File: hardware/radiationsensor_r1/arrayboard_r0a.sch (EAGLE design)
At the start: 19 parts, among them CN0 RADIATION-SENSOR-REV1, CN1 RADIATION-SENSOR-REV1, CN10 RADIATION-SENSOR-REV1, CN11 RADIATION-SENSOR-REV1, CN12 RADIATION-SENSOR-REV1, CN13 RADIATION-SENSOR-REV1, CN14 RADIATION-SENSOR-REV1, CN15 RADIATION-SENSOR-REV1, CN2 RADIATION-SENSOR-REV1, CN3 RADIATION-SENSOR-REV1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

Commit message: basic layout (not including microcontroller)
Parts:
- removed U$17: ARDUINO_PRO_MINI, SparkFun-Boards:ARDUINO_PRO_MINI
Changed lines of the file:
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@@
 <layer number="54" name="bGND_GNDA" color="1" fill="9" visible="no" active="no"/>
 <layer number="56" name="wert" color="7" fill="1" visible="no" active="no"/>
+<layer number="57" name="tCAD" color="7" fill="1" visible="no" active="no"/>
 <layer number="91" name="Nets" color="2" fill="1" visible="yes" active="yes"/>
 <layer number="92" name="Busses" color="1" fill="1" visible="yes" active="yes"/>
@@
 <layer number="132" name="bAdjust" color="7" fill="1" visible="yes" active="yes"/>
 <layer number="144" name="Drill_legend" color="7" fill="1" visible="no" active="yes"/>
+<layer number="150" name="Notes" color="7" fill="1" visible="no" active="yes"/>
 <layer number="151" name="HeatSink" color="7" fill="1" visible="no" active="yes"/>
 <layer number="152" name="_bDocu" color="7" fill="1" visible="yes" active="yes"/>
+<layer number="153" name="FabDoc1" color="6" fill="1" visible="no" active="no"/>
+<layer number="154" name="FabDoc2" color="2" fill="1" visible="no" active="no"/>
+<layer number="155" name="FabDoc3" color="7" fill="15" visible="no" active="no"/>
 <layer number="199" name="Contour" color="7" fill="1" visible="yes" active="yes"/>
 <layer number="200" name="200bmp" color="1" fill="10" visible="no" active="yes"/>
@@
 <part name="CN14" library="openct" deviceset="RADIATION-SENSOR-REV1" device=""/>
 <part name="CN15" library="openct" deviceset="RADIATION-SENSOR-REV1" device=""/>
-<part name="U$17" library="SparkFun-Boards" deviceset="ARDUINO_PRO_MINI" device=""/>
 <part name="GND1" library="openct" deviceset="GND" device=""/>
 <part name="GND2" library="openct" deviceset="GND" device=""/>
@@
 <instance part="CN14" gate="G$1" x="78.74" y="-198.12"/>
 <instance part="CN15" gate="G$1" x="78.74" y="-236.22"/>
-<instance part="U$17" gate="G$1" x="-63.5" y="25.4"/>
 <instance part="GND1" gate="1" x="50.8" y="12.7"/>
 <instance part="GND2" gate="1" x="114.3" y="12.7"/>

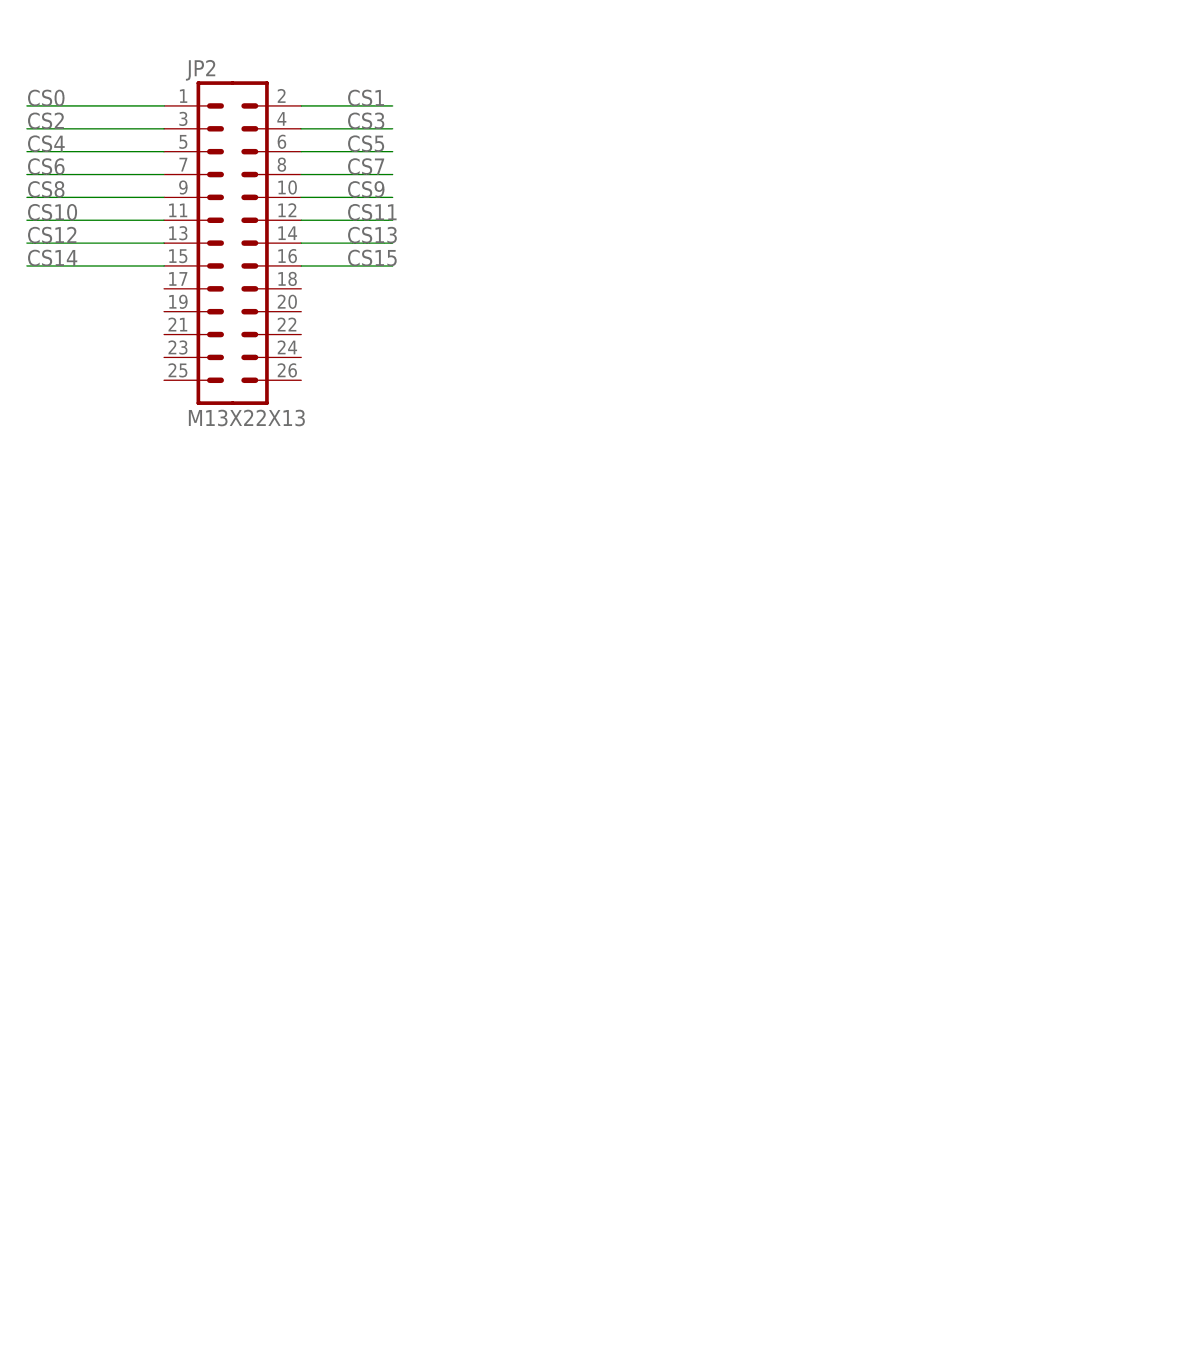
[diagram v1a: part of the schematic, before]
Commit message: Added connector an IO expander
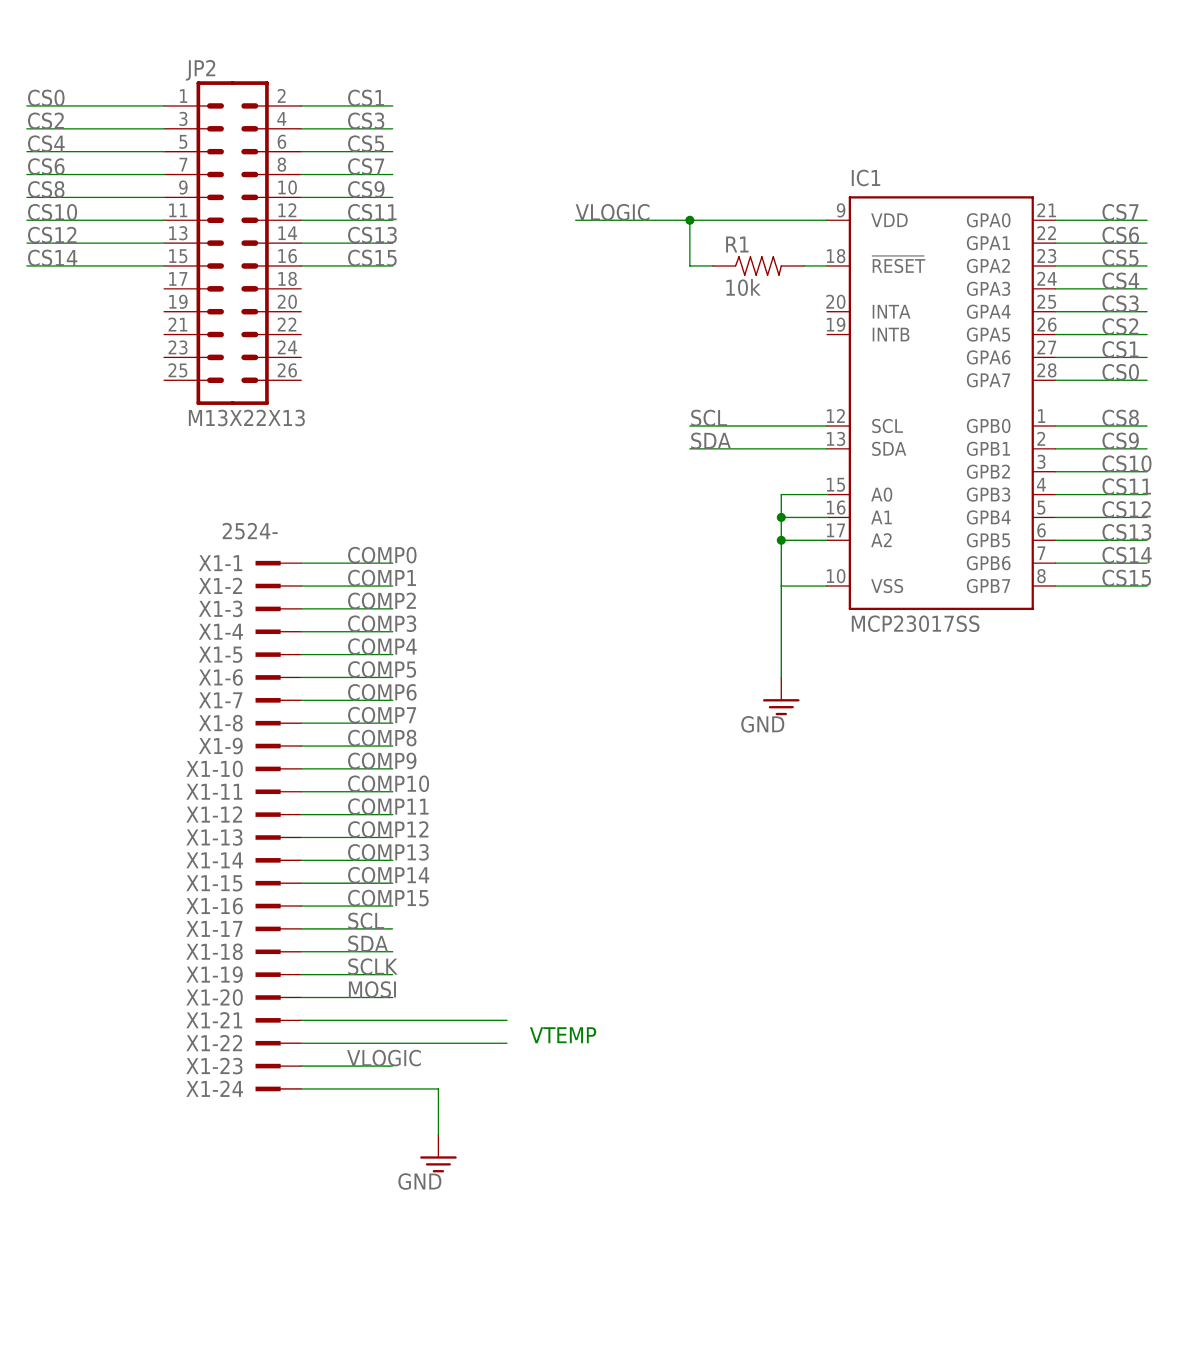
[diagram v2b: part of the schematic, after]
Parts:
- added IC1: MCP23017SS, adafruit:MCP23017SS
- added R1: 10k, openct:RESISTOR0603
- added X1: 2524-, con-3m:2524-
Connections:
- new net N$19: X1-21.KL
- new net N$2: IC1.!RESET, R1.2
- new net N$20: X1-22.KL
- new net SCL: IC1.SCL, X1-17.KL
- new net SDA: IC1.SDA, X1-18.KL
- new net VLOGIC: IC1.VDD, R1.1, X1-23.KL
- net COMP0: now also X1-1.KL
- net COMP1: now also X1-2.KL
- net COMP10: now also X1-11.KL
- net COMP11: now also X1-12.KL
- net COMP12: now also X1-13.KL
- net COMP13: now also X1-14.KL
- net COMP14: now also X1-15.KL
- net COMP15: now also X1-16.KL
- net COMP2: now also X1-3.KL
- net COMP3: now also X1-4.KL
- net COMP4: now also X1-5.KL
- net COMP5: now also X1-6.KL
- net COMP6: now also X1-7.KL
- net COMP7: now also X1-8.KL
- net COMP8: now also X1-9.KL
- net COMP9: now also X1-10.KL
- net CS0: now also IC1.GPA7
- net CS1: now also IC1.GPA6
- net CS10: now also IC1.GPB2
- net CS11: now also IC1.GPB3
- net CS12: now also IC1.GPB4
- net CS13: now also IC1.GPB5
- net CS14: now also IC1.GPB6
- net CS15: now also IC1.GPB7
- net CS2: now also IC1.GPA5
- net CS3: now also IC1.GPA4
- net CS4: now also IC1.GPA3
- net CS5: now also IC1.GPA2
- net CS6: now also IC1.GPA1
- net CS7: now also IC1.GPA0
- net CS8: now also IC1.GPB0
- net CS9: now also IC1.GPB1
- net GND: now also IC1.A0, IC1.A1, IC1.A2, IC1.VSS, X1-24.KL
- net MOSI: now also X1-20.KL
- net SCLK: now also X1-19.KL
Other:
- note added: "VTEMP"

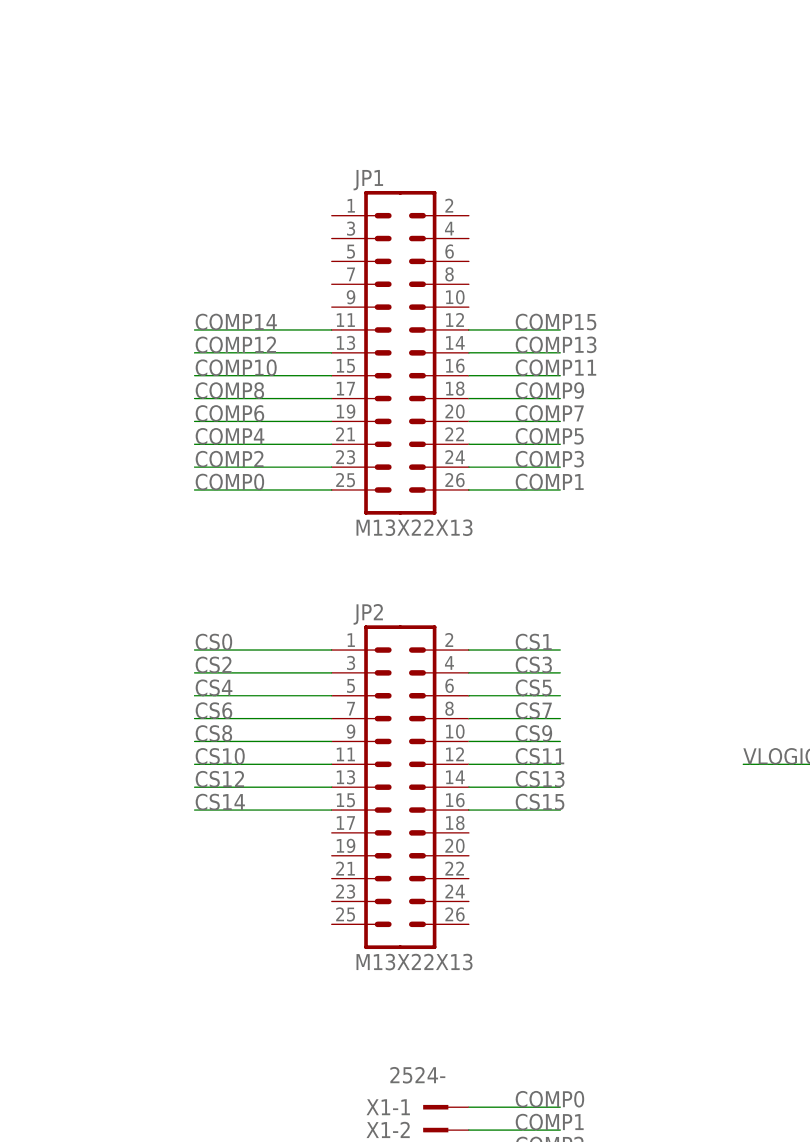
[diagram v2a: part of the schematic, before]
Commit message: connector and IO expander nearly wired
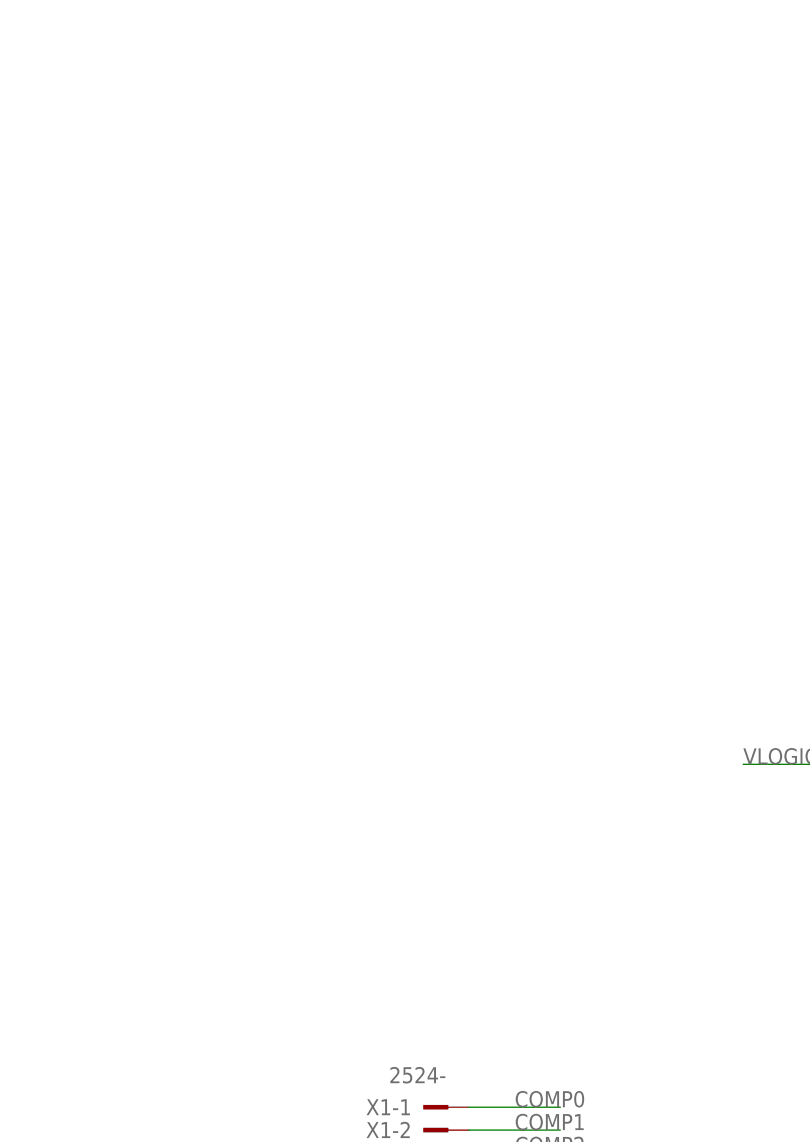
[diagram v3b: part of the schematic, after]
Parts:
- removed JP1, JP2: M13X22X13, SparkFun-Connectors:M13X22X13
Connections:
- net COMP0: no longer JP1.25
- net COMP1: no longer JP1.26
- net COMP10: no longer JP1.15
- net COMP11: no longer JP1.16
- net COMP12: no longer JP1.13
- net COMP13: no longer JP1.14
- net COMP14: no longer JP1.11
- net COMP15: no longer JP1.12
- net COMP2: no longer JP1.23
- net COMP3: no longer JP1.24
- net COMP4: no longer JP1.21
- net COMP5: no longer JP1.22
- net COMP6: no longer JP1.19
- net COMP7: no longer JP1.20
- net COMP8: no longer JP1.17
- net COMP9: no longer JP1.18
- net CS0: no longer JP2.1
- net CS1: no longer JP2.2
- net CS10: no longer JP2.11
- net CS11: no longer JP2.12
- net CS12: no longer JP2.13
- net CS13: no longer JP2.14
- net CS14: no longer JP2.15
- net CS15: no longer JP2.16
- net CS2: no longer JP2.3
- net CS3: no longer JP2.4
- net CS4: no longer JP2.5
- net CS5: no longer JP2.6
- net CS6: no longer JP2.7
- net CS7: no longer JP2.8
- net CS8: no longer JP2.9
- net CS9: no longer JP2.10

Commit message: basic layout complete
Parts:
- added C1: (no value), openct:CAP0603
- added X2: 22-23-2041, con-molex:22-23-2041
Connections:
- removed net N$19: X1-21.KL
- removed net N$20: X1-22.KL
- new net VTEMP11: CN11.VTEMP, X1-22.KL
- new net VTEMP4: CN4.VTEMP, X1-21.KL
- net 5V: now also X2-1.S
- net GND: now also C1.2, X2-2.S, X2-3.S
- net VBIAS: now also X2-4.S
- net VLOGIC: now also C1.1
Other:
- note removed: "VTEMP"
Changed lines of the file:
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@@
 <part name="GND18" library="openct" deviceset="GND" device=""/>
 <part name="R1" library="openct" deviceset="RESISTOR" device="0603" value="10k"/>
+<part name="C1" library="openct" deviceset="CAP" device="0603"/>
+<part name="GND19" library="openct" deviceset="GND" device=""/>
+<part name="X2" library="con-molex" deviceset="22-23-2041" device=""/>
+<part name="U$17" library="openct" deviceset="VBIAS" device=""/>
+<part name="U$34" library="openct" deviceset="5V" device=""/>
+<part name="GND20" library="openct" deviceset="GND" device=""/>
 </parts>
 <sheets>
 <sheet>
 <plain>
-<text x="231.14" y="-205.74" size="1.778" layer="91">VTEMP</text>
 </plain>
 <instances>
@@
 <instance part="GND18" gate="1" x="259.08" y="-167.64"/>
 <instance part="R1" gate="G$1" x="256.54" y="-119.38"/>
+<instance part="C1" gate="G$1" x="241.3" y="-119.38"/>
+<instance part="GND19" gate="1" x="241.3" y="-124.46"/>
+<instance part="X2" gate="-1" x="200.66" y="-248.92" rot="R180"/>
+<instance part="X2" gate="-2" x="200.66" y="-246.38" rot="R180"/>
+<instance part="X2" gate="-3" x="200.66" y="-243.84" rot="R180"/>
+<instance part="X2" gate="-4" x="200.66" y="-241.3" rot="R180"/>
+<instance part="U$17" gate="G$1" x="208.28" y="-236.22"/>
+<instance part="U$34" gate="G$1" x="208.28" y="-254" rot="R180"/>
+<instance part="GND20" gate="1" x="220.98" y="-254"/>
 </instances>
 <busses>
@@
 <junction x="259.08" y="-149.86"/>
 </segment>
+<segment>
+<pinref part="C1" gate="G$1" pin="2"/>
+<pinref part="GND19" gate="1" pin="GND"/>
+</segment>
+<segment>
+<pinref part="X2" gate="-2" pin="S"/>
+<wire x1="203.2" y1="-246.38" x2="208.28" y2="-246.38" width="0.1524" layer="91"/>
+<wire x1="208.28" y1="-246.38" x2="208.28" y2="-243.84" width="0.1524" layer="91"/>
+<wire x1="208.28" y1="-243.84" x2="220.98" y2="-243.84" width="0.1524" layer="91"/>
+<wire x1="220.98" y1="-243.84" x2="220.98" y2="-251.46" width="0.1524" layer="91"/>
+<pinref part="X2" gate="-3" pin="S"/>
+<wire x1="203.2" y1="-243.84" x2="208.28" y2="-243.84" width="0.1524" layer="91"/>
+<junction x="208.28" y="-243.84"/>
+<pinref part="GND20" gate="1" pin="GND"/>
+</segment>
 </net>
 <net name="5V" class="0">
@@
 <pinref part="U$16" gate="G$1" pin="5V"/>
 </segment>
+<segment>
+<pinref part="X2" gate="-1" pin="S"/>
+<wire x1="203.2" y1="-248.92" x2="208.28" y2="-248.92" width="0.1524" layer="91"/>
+<wire x1="208.28" y1="-248.92" x2="208.28" y2="-254" width="0.1524" layer="91"/>
+<pinref part="U$34" gate="G$1" pin="5V"/>
+</segment>
 </net>
 <net name="VBIAS" class="0">
@@
 <pinref part="U$33" gate="G$1" pin="VBIAS"/>
 </segment>
+<segment>
+<pinref part="X2" gate="-4" pin="S"/>
+<wire x1="203.2" y1="-241.3" x2="208.28" y2="-241.3" width="0.1524" layer="91"/>
+<wire x1="208.28" y1="-241.3" x2="208.28" y2="-236.22" width="0.1524" layer="91"/>
+<pinref part="U$17" gate="G$1" pin="VBIAS"/>
+</segment>
 </net>
 <net name="CS0" class="0">
@@
 </segment>
 </net>
-<net name="N$19" class="0">
+<net name="VTEMP4" class="0">
 <segment>
 <pinref part="X1" gate="-21" pin="KL"/>
-<wire x1="205.74" y1="-203.2" x2="228.6" y2="-203.2" width="0.1524" layer="91"/>
-</segment>
-</net>
-<net name="N$20" class="0">
+<wire x1="205.74" y1="-203.2" x2="215.9" y2="-203.2" width="0.1524" layer="91"/>
+<label x="210.82" y="-203.2" size="1.778" layer="95"/>
+</segment>
+<segment>
+<pinref part="CN4" gate="G$1" pin="VTEMP"/>
+<wire x1="27.94" y1="-111.76" x2="38.1" y2="-111.76" width="0.1524" layer="91"/>
+<label x="33.02" y="-111.76" size="1.778" layer="95"/>
+</segment>
+</net>
+<net name="VTEMP11" class="0">
 <segment>
 <pinref part="X1" gate="-22" pin="KL"/>
-<wire x1="205.74" y1="-205.74" x2="228.6" y2="-205.74" width="0.1524" layer="91"/>
+<wire x1="205.74" y1="-205.74" x2="215.9" y2="-205.74" width="0.1524" layer="91"/>
+<label x="210.82" y="-205.74" size="1.778" layer="95"/>
+</segment>
+<segment>
+<pinref part="CN11" gate="G$1" pin="VTEMP"/>
+<wire x1="91.44" y1="-73.66" x2="101.6" y2="-73.66" width="0.1524" layer="91"/>
+<label x="96.52" y="-73.66" size="1.778" layer="95"/>
 </segment>
 </net>
@@
 <label x="236.22" y="-114.3" size="1.778" layer="95"/>
 <pinref part="R1" gate="G$1" pin="1"/>
-<wire x1="248.92" y1="-114.3" x2="236.22" y2="-114.3" width="0.1524" layer="91"/>
+<wire x1="248.92" y1="-114.3" x2="241.3" y2="-114.3" width="0.1524" layer="91"/>
+<wire x1="241.3" y1="-114.3" x2="236.22" y2="-114.3" width="0.1524" layer="91"/>
 <wire x1="251.46" y1="-119.38" x2="248.92" y2="-119.38" width="0.1524" layer="91"/>
 <wire x1="248.92" y1="-119.38" x2="248.92" y2="-114.3" width="0.1524" layer="91"/>
 <junction x="248.92" y="-114.3"/>
-</segment>
-</net>
+<pinref part="C1" gate="G$1" pin="1"/>
+<junction x="241.3" y="-114.3"/>
+</segment>
+</net>

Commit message: mechanical bits
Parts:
- renumbered IC1 to U1, X1 to CN16, X2 to CN17
